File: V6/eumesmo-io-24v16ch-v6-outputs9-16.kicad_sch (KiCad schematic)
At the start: 5 parts, among them Q12 MMBT2222A

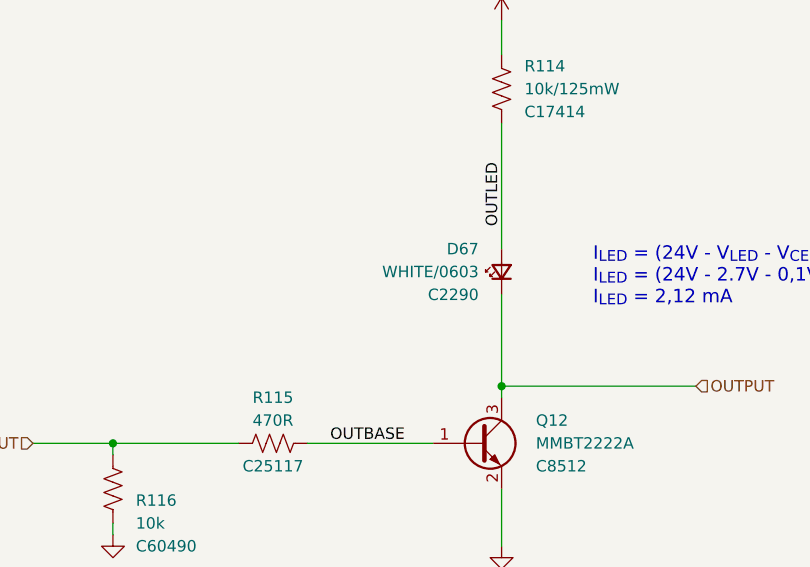
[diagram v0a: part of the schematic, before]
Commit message: Replaced white leds for emerald.
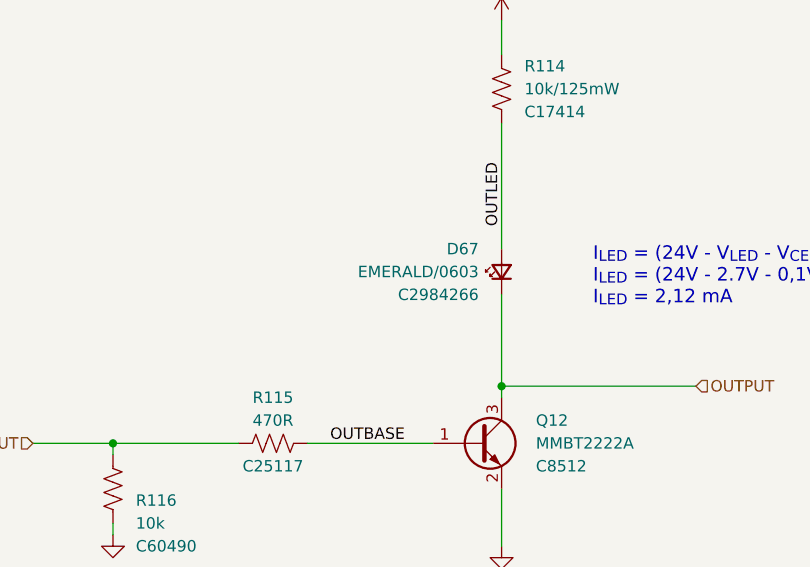
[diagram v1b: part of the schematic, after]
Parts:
- D67: value WHITE/0603 -> EMERALD/0603; LCSC Part # C2290 -> C2984266; Mfr Hubei KENTO Elec -> Everlight Elec; Mfr PN KT-0603W -> 19-213/GHC-XS1T1N/5T; Technology (none) -> LED; Vendor PN C2290 -> C2984266
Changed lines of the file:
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@@
 			)
 		)
-		(property "Value" "WHITE/0603"
+		(property "Value" "EMERALD/0603"
 			(at 142.24 82.55 90)
 			(show_name no)
@@
 			)
 		)
-		(property "Mfr" "Hubei KENTO Elec"
+		(property "Mfr" "Everlight Elec"
 			(at 144.78 82.55 0)
 			(hide yes)
@@
 			)
 		)
-		(property "Mfr PN" "KT-0603W"
+		(property "Mfr PN" "19-213/GHC-XS1T1N/5T"
 			(at 144.78 82.55 0)
 			(hide yes)
@@
 			)
 		)
-		(property "Technology" ""
+		(property "Technology" "LED"
 			(at 144.78 82.55 0)
 			(hide yes)
@@
 			)
 		)
-		(property "Vendor PN" "C2290"
+		(property "Vendor PN" "C2984266"
 			(at 144.78 82.55 0)
 			(hide yes)
@@
 			)
 		)
-		(property "LCSC Part #" "C2290"
+		(property "LCSC Part #" "C2984266"
 			(at 142.24 85.09 90)
 			(show_name no)

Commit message: Remove jumpers from BOM.
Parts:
- D67: FT Rotation Offset 0 -> 180
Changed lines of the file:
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@@
 			)
 		)
-		(property "FT Rotation Offset" "0"
+		(property "FT Rotation Offset" "180"
 			(at 144.78 82.55 90)
 			(hide yes)

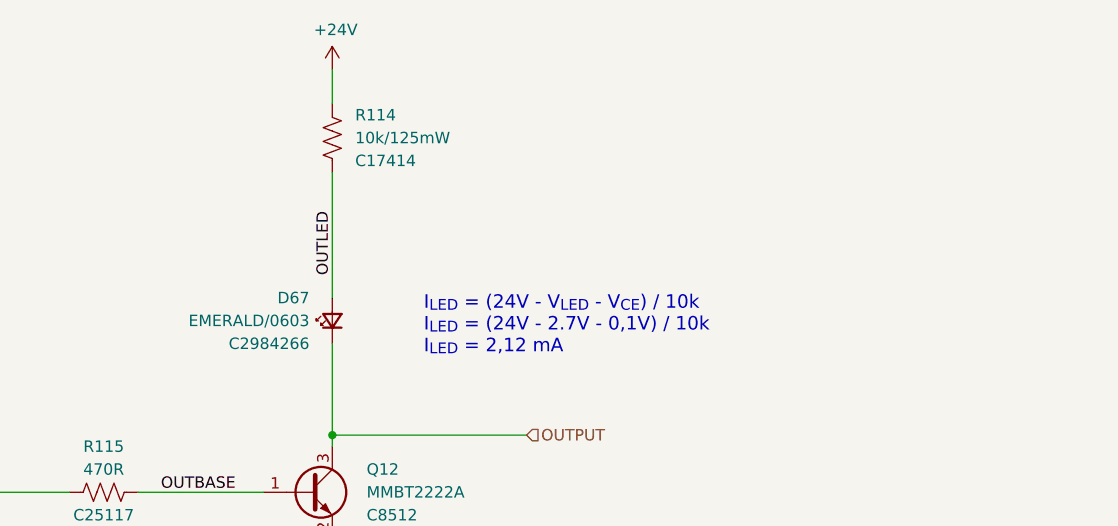
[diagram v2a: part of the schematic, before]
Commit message: LEDs changed to orange
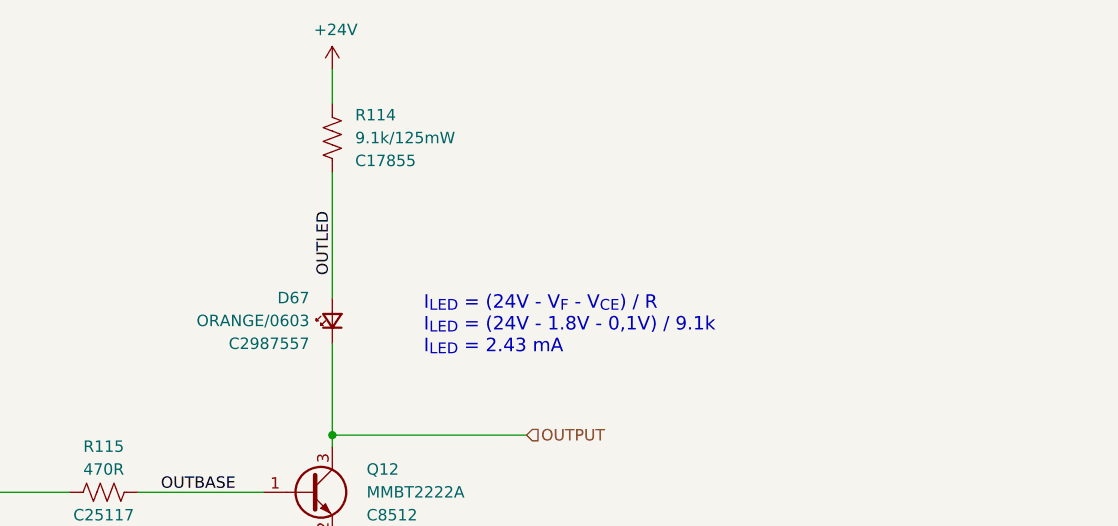
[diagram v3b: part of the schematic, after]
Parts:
- D67: value EMERALD/0603 -> ORANGE/0603; FT Rotation Offset 180 -> 0; LCSC Part # C2984266 -> C2987557; Mfr PN 19-213/GHC-XS1T1N/5T -> 19-217/S2C-AL1M2VY/6T; Vendor PN C2984266 -> C2987557
- R114: value 10k/125mW -> 9.1k/125mW; LCSC Part # C17414 -> C17855; Mfr PN 0805W8F1002T5E -> 0805W8F9101T5E; Vendor PN C17414 -> C17855
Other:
- note added: "I_{LED} = (24V - V_{F} - V_{CE}) / R I_{LED} = (24V - 1.8V - 0,1V) / 9.1k I_{LED} = 2.43 mA"
- note removed: "I_{LED} = (24V - V_{LED} - V_{CE}) / 10k I_{LED} = (24V - 2.7V - 0,1V) / 10k I_{LED} = 2,12 mA"
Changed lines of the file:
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@@
 		)
 	)
-	(text "I_{LED} = (24V - V_{LED} - V_{CE}) / 10k\nI_{LED} = (24V - 2.7V - 0,1V) / 10k\nI_{LED} = 2,12 mA"
+	(text "I_{LED} = (24V - V_{F} - V_{CE}) / R\nI_{LED} = (24V - 1.8V - 0,1V) / 9.1k\nI_{LED} = 2.43 mA"
 		(exclude_from_sim no)
 		(at 154.94 86.36 0)
@@
 			)
 		)
-		(property "Value" "EMERALD/0603"
+		(property "Value" "ORANGE/0603"
 			(at 142.24 82.55 90)
 			(show_name no)
@@
 			)
 		)
-		(property "Mfr PN" "19-213/GHC-XS1T1N/5T"
+		(property "Mfr PN" "19-217/S2C-AL1M2VY/6T"
 			(at 144.78 82.55 0)
 			(hide yes)
@@
 			)
 		)
-		(property "Vendor PN" "C2984266"
+		(property "Vendor PN" "C2987557"
 			(at 144.78 82.55 0)
 			(hide yes)
@@
 			)
 		)
-		(property "LCSC Part #" "C2984266"
+		(property "LCSC Part #" "C2987557"
 			(at 142.24 85.09 90)
 			(show_name no)
@@
 			)
 		)
-		(property "FT Rotation Offset" "180"
+		(property "FT Rotation Offset" "0"
 			(at 144.78 82.55 90)
 			(hide yes)
@@
 			)
 		)
-		(property "Value" "10k/125mW"
+		(property "Value" "9.1k/125mW"
 			(at 147.32 62.23 0)
 			(show_name no)
@@
 			)
 		)
-		(property "Mfr PN" "0805W8F1002T5E"
+		(property "Mfr PN" "0805W8F9101T5E"
 			(at 144.78 62.23 0)
 			(hide yes)
@@
 			)
 		)
-		(property "Vendor PN" "C17414"
+		(property "Vendor PN" "C17855"
 			(at 144.78 62.23 0)
 			(hide yes)
@@
 			)
 		)
-		(property "LCSC Part #" "C17414"
+		(property "LCSC Part #" "C17855"
 			(at 147.32 64.77 0)
 			(show_name no)

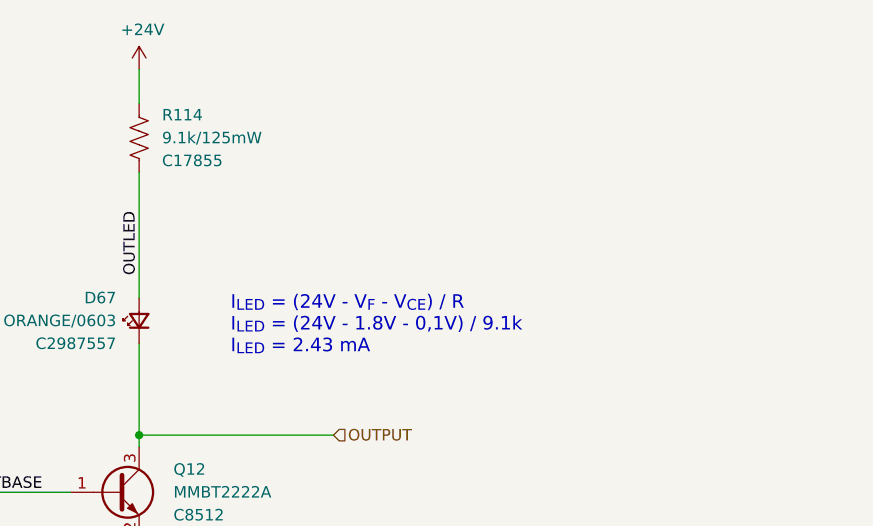
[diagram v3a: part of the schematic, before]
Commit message: LEDs replaced for orange
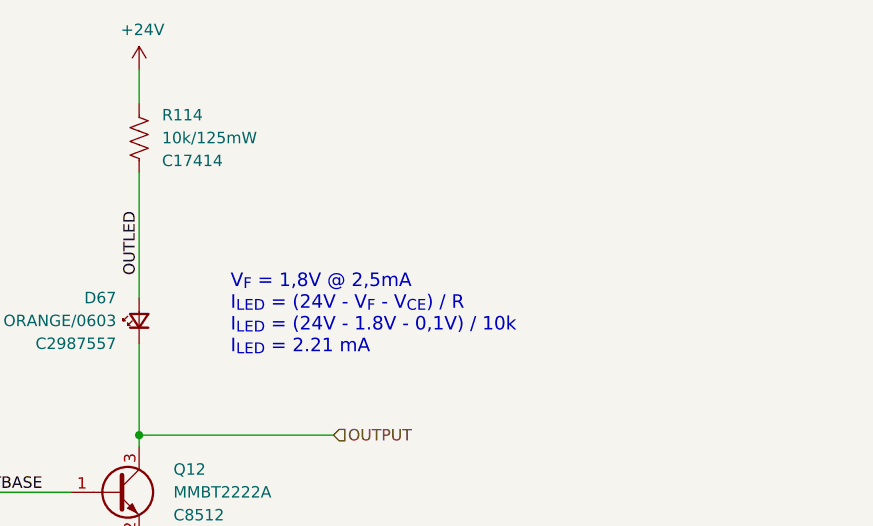
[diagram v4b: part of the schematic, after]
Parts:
- R114: value 9.1k/125mW -> 10k/125mW; LCSC Part # C17855 -> C17414; Mfr PN 0805W8F9101T5E -> 0805W8F1002T5E; Vendor PN C17855 -> C17414
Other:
- note added: "V_{F} = 1,8V @ 2,5mA I_{LED} = (24V - V_{F} - V_{CE}) / R I_{LED} = (24V - 1.8V - 0,1V) / 10k I_{LED} = 2.21 mA"
- note removed: "I_{LED} = (24V - V_{F} - V_{CE}) / R I_{LED} = (24V - 1.8V - 0,1V) / 9.1k I_{LED} = 2.43 mA"
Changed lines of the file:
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@@
 		)
 	)
-	(text "I_{LED} = (24V - V_{F} - V_{CE}) / R\nI_{LED} = (24V - 1.8V - 0,1V) / 9.1k\nI_{LED} = 2.43 mA"
+	(text "V_{F} = 1,8V @ 2,5mA\nI_{LED} = (24V - V_{F} - V_{CE}) / R\nI_{LED} = (24V - 1.8V - 0,1V) / 10k\nI_{LED} = 2.21 mA"
 		(exclude_from_sim no)
 		(at 154.94 86.36 0)
@@
 			)
 		)
-		(property "Value" "9.1k/125mW"
+		(property "Value" "10k/125mW"
 			(at 147.32 62.23 0)
 			(show_name no)
@@
 			)
 		)
-		(property "Mfr PN" "0805W8F9101T5E"
+		(property "Mfr PN" "0805W8F1002T5E"
 			(at 144.78 62.23 0)
 			(hide yes)
@@
 			)
 		)
-		(property "Vendor PN" "C17855"
+		(property "Vendor PN" "C17414"
 			(at 144.78 62.23 0)
 			(hide yes)
@@
 			)
 		)
-		(property "LCSC Part #" "C17855"
+		(property "LCSC Part #" "C17414"
 			(at 147.32 64.77 0)
 			(show_name no)
